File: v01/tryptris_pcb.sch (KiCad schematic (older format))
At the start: 135 parts

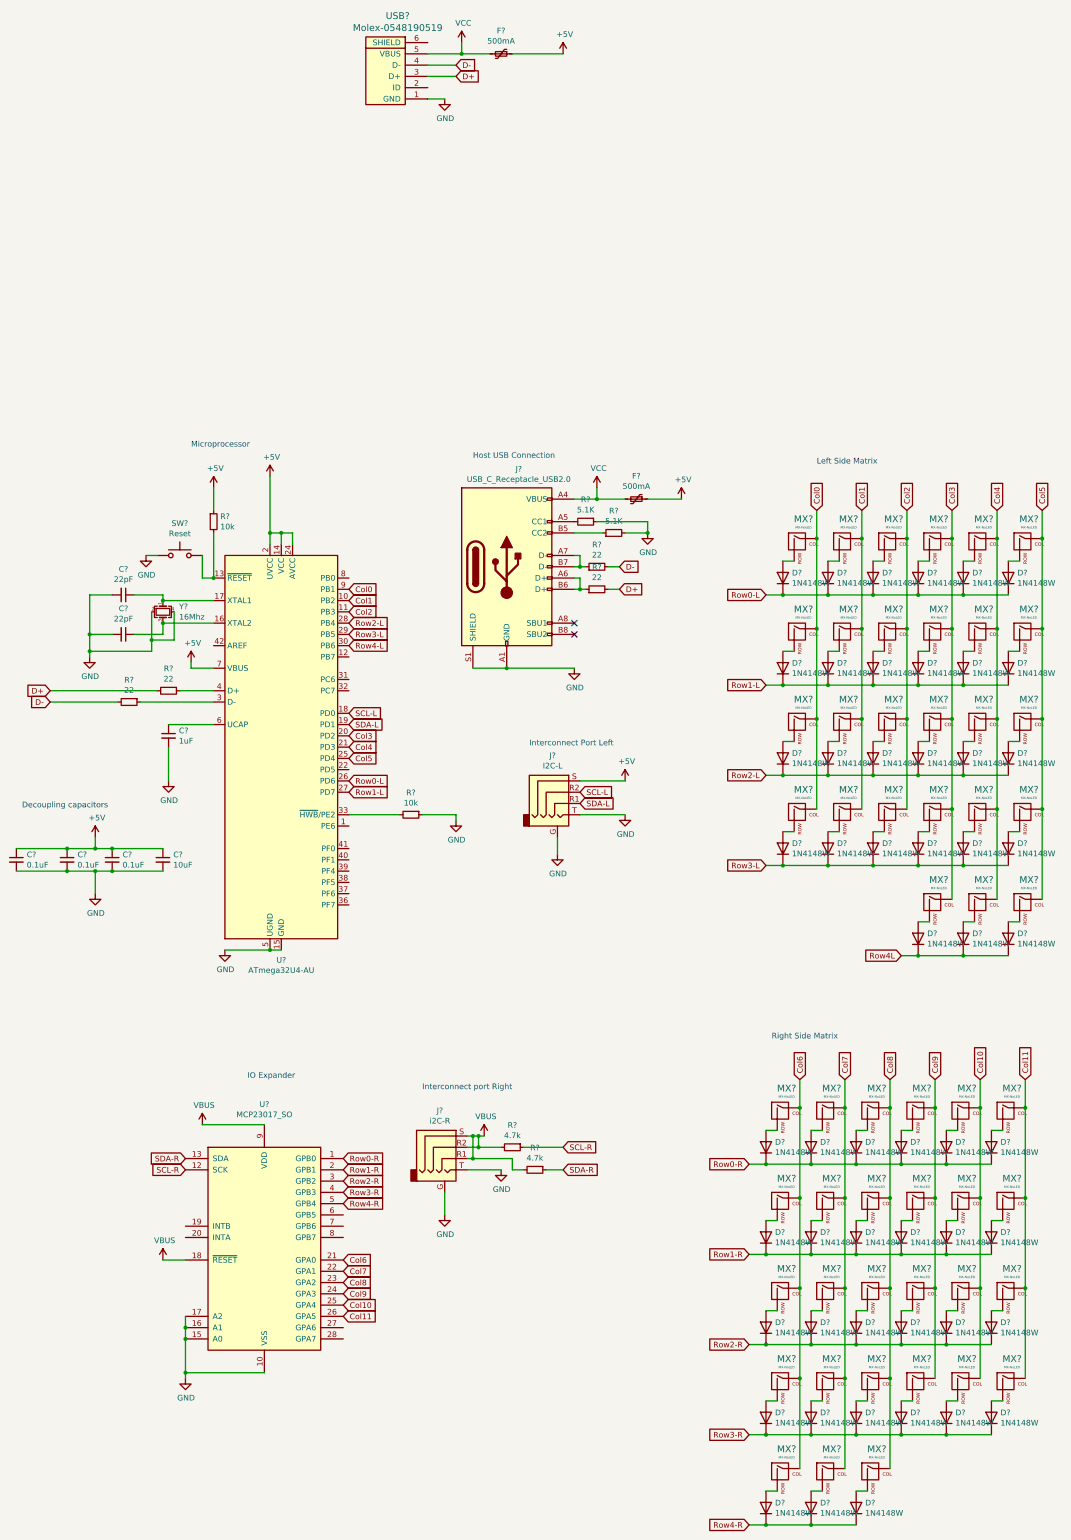
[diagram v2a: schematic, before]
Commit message: Started left side of PCB
* Got switches and diodes for the left side placed.
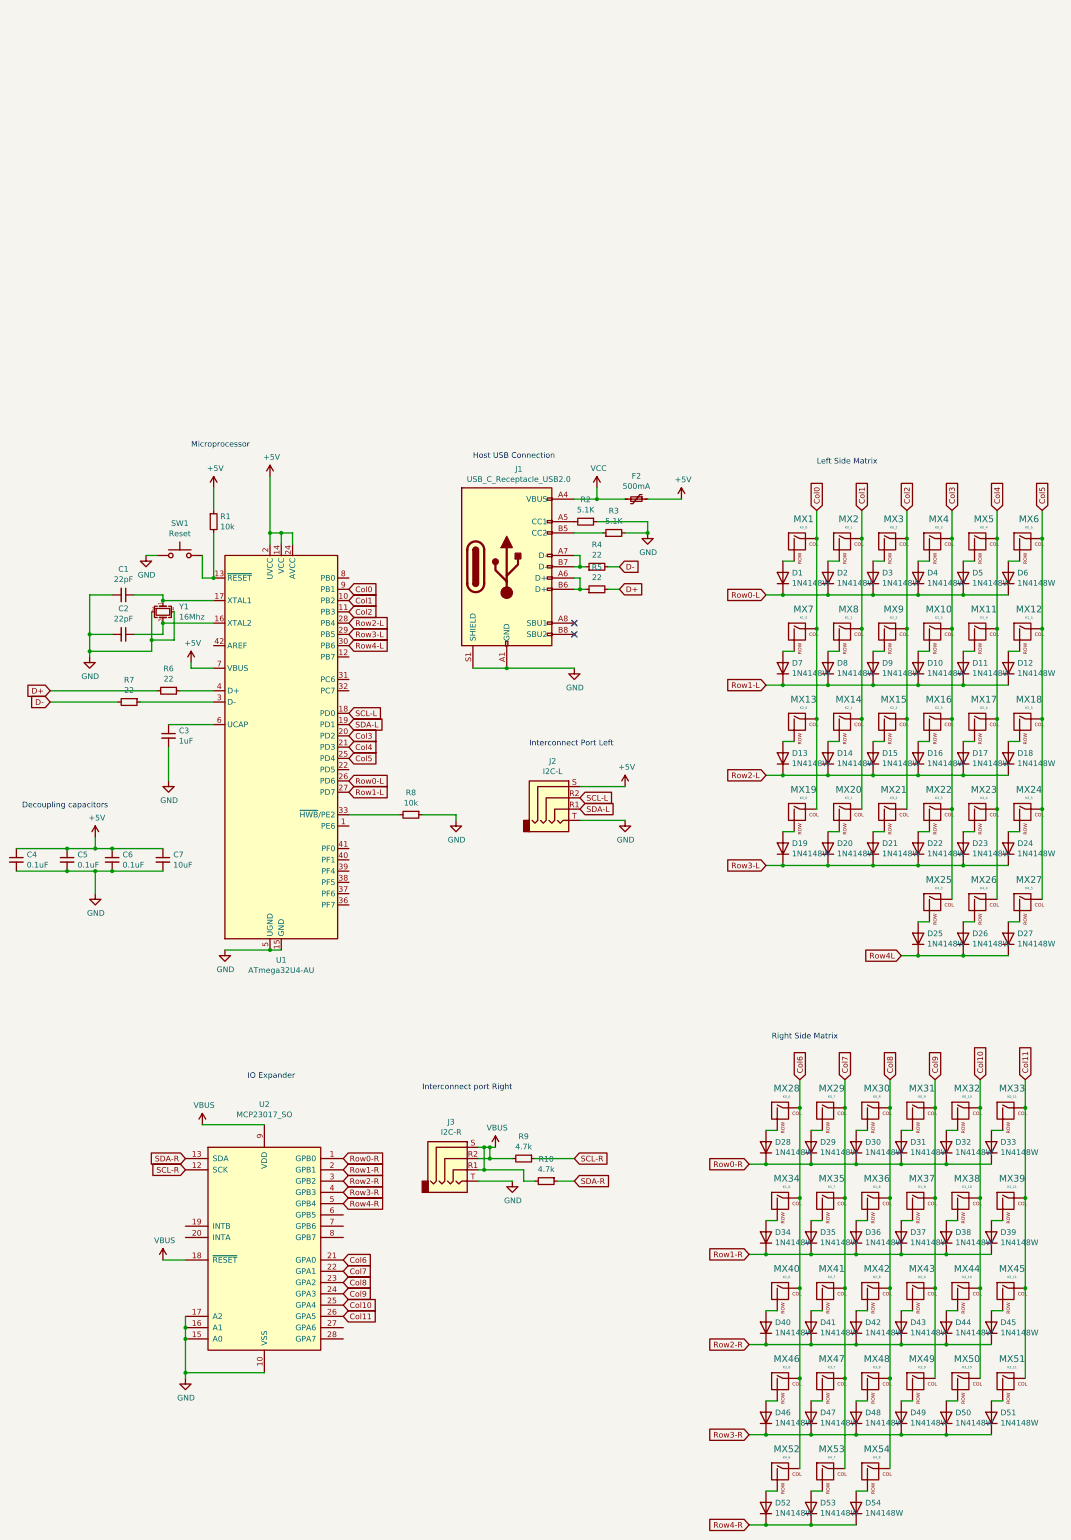
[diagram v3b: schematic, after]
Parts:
- removed F?: 500mA, symbol Device:Polyfuse_Small
- removed J?: i2C-R, symbol Connector:AudioJack4_Ground
- removed J?: I2C-L, symbol Connector:AudioJack4_Ground
- removed USB?: Molex-0548190519, symbol random-keyboard-parts:Molex-0548190519
- added J2: I2C-L, Connector_Audio:Jack_3.5mm_PJ320E_Horizontal, symbol Connector:AudioJack4
- added J3: I2C-R, Connector_Audio:Jack_3.5mm_PJ320E_Horizontal, symbol Connector:AudioJack4
- C1, C2, C3, C4, C5, C6, C7: renamed from C?; footprint (none) -> Capacitor_SMD:C_0805_2012Metric
- F2: renamed from F?; footprint (none) -> Fuse:Fuse_1206_3216Metric
- J1: renamed from J?; footprint (none) -> Type-C:USB_C_GCT_USB4085
- MX1: renamed from MX?; value MX-NoLED -> K0_0; footprint (none) -> MX_Only:MXOnly-1U-NoLED
- MX10: renamed from MX?; value MX-NoLED -> K1_3; footprint (none) -> MX_Only:MXOnly-1U-NoLED
- MX11: renamed from MX?; value MX-NoLED -> K1_4; footprint (none) -> MX_Only:MXOnly-1U-NoLED
- MX12: renamed from MX?; value MX-NoLED -> K1_5; footprint (none) -> MX_Only:MXOnly-1U-NoLED
- MX13: renamed from MX?; value MX-NoLED -> K2_0; footprint (none) -> MX_Only:MXOnly-1U-NoLED
- MX14: renamed from MX?; value MX-NoLED -> K2_1; footprint (none) -> MX_Only:MXOnly-1U-NoLED
- MX15: renamed from MX?; value MX-NoLED -> K2_2; footprint (none) -> MX_Only:MXOnly-1U-NoLED
- MX16: renamed from MX?; value MX-NoLED -> K2_3; footprint (none) -> MX_Only:MXOnly-1U-NoLED
- MX17: renamed from MX?; value MX-NoLED -> K2_4; footprint (none) -> MX_Only:MXOnly-1U-NoLED
- MX18: renamed from MX?; value MX-NoLED -> K2_5; footprint (none) -> MX_Only:MXOnly-1U-NoLED
- MX19: renamed from MX?; value MX-NoLED -> K3_0; footprint (none) -> MX_Only:MXOnly-1U-NoLED
- MX2: renamed from MX?; value MX-NoLED -> K0_1; footprint (none) -> MX_Only:MXOnly-1U-NoLED
- MX20: renamed from MX?; value MX-NoLED -> K3_1; footprint (none) -> MX_Only:MXOnly-1U-NoLED
- MX21: renamed from MX?; value MX-NoLED -> K3_2; footprint (none) -> MX_Only:MXOnly-1U-NoLED
- MX22: renamed from MX?; value MX-NoLED -> K3_3; footprint (none) -> MX_Only:MXOnly-1U-NoLED
- MX23: renamed from MX?; value MX-NoLED -> K3_4; footprint (none) -> MX_Only:MXOnly-1U-NoLED
- MX24: renamed from MX?; value MX-NoLED -> K3_5; footprint (none) -> MX_Only:MXOnly-1U-NoLED
- MX25: renamed from MX?; value MX-NoLED -> K4_3; footprint (none) -> MX_Only:MXOnly-1U-NoLED
- MX26: renamed from MX?; value MX-NoLED -> K4_4; footprint (none) -> MX_Only:MXOnly-1U-NoLED
- MX27: renamed from MX?; value MX-NoLED -> K4_5; footprint (none) -> MX_Only:MXOnly-1U-NoLED
- MX28: renamed from MX?; value MX-NoLED -> K0_6; footprint (none) -> MX_Only:MXOnly-1U-NoLED
- MX29: renamed from MX?; value MX-NoLED -> K0_7; footprint (none) -> MX_Only:MXOnly-1U-NoLED
- MX3: renamed from MX?; value MX-NoLED -> K0_2; footprint (none) -> MX_Only:MXOnly-1U-NoLED
- MX30: renamed from MX?; value MX-NoLED -> K0_8; footprint (none) -> MX_Only:MXOnly-1U-NoLED
- MX31: renamed from MX?; value MX-NoLED -> K0_9; footprint (none) -> MX_Only:MXOnly-1U-NoLED
- MX32: renamed from MX?; value MX-NoLED -> K0_10; footprint (none) -> MX_Only:MXOnly-1U-NoLED
- MX33: renamed from MX?; value MX-NoLED -> K0_11; footprint (none) -> MX_Only:MXOnly-1U-NoLED
- MX34: renamed from MX?; value MX-NoLED -> K1_6; footprint (none) -> MX_Only:MXOnly-1U-NoLED
- MX35: renamed from MX?; value MX-NoLED -> K1_7; footprint (none) -> MX_Only:MXOnly-1U-NoLED
- MX36: renamed from MX?; value MX-NoLED -> K1_8; footprint (none) -> MX_Only:MXOnly-1U-NoLED
- MX37: renamed from MX?; value MX-NoLED -> K1_9; footprint (none) -> MX_Only:MXOnly-1U-NoLED
- MX38: renamed from MX?; value MX-NoLED -> K1_10; footprint (none) -> MX_Only:MXOnly-1U-NoLED
- MX39: renamed from MX?; value MX-NoLED -> K1_11; footprint (none) -> MX_Only:MXOnly-1U-NoLED
- MX4: renamed from MX?; value MX-NoLED -> K0_3; footprint (none) -> MX_Only:MXOnly-1U-NoLED
- MX40: renamed from MX?; value MX-NoLED -> K2_6; footprint (none) -> MX_Only:MXOnly-1U-NoLED
- MX41: renamed from MX?; value MX-NoLED -> K2_7; footprint (none) -> MX_Only:MXOnly-1U-NoLED
- MX42: renamed from MX?; value MX-NoLED -> K2_8; footprint (none) -> MX_Only:MXOnly-1U-NoLED
- MX43: renamed from MX?; value MX-NoLED -> K2_9; footprint (none) -> MX_Only:MXOnly-1U-NoLED
- MX44: renamed from MX?; value MX-NoLED -> K2_10; footprint (none) -> MX_Only:MXOnly-1U-NoLED
- MX45: renamed from MX?; value MX-NoLED -> K2_11; footprint (none) -> MX_Only:MXOnly-1U-NoLED
- MX46: renamed from MX?; value MX-NoLED -> K3_6; footprint (none) -> MX_Only:MXOnly-1U-NoLED
- MX47: renamed from MX?; value MX-NoLED -> K3_7; footprint (none) -> MX_Only:MXOnly-1U-NoLED
- MX48: renamed from MX?; value MX-NoLED -> K3_8; footprint (none) -> MX_Only:MXOnly-1U-NoLED
- MX49: renamed from MX?; value MX-NoLED -> K3_9; footprint (none) -> MX_Only:MXOnly-1U-NoLED
- MX5: renamed from MX?; value MX-NoLED -> K0_4; footprint (none) -> MX_Only:MXOnly-1U-NoLED
- MX50: renamed from MX?; value MX-NoLED -> K3_10; footprint (none) -> MX_Only:MXOnly-1U-NoLED
- MX51: renamed from MX?; value MX-NoLED -> K3_11; footprint (none) -> MX_Only:MXOnly-1U-NoLED
- MX52: renamed from MX?; value MX-NoLED -> K4_6; footprint (none) -> MX_Only:MXOnly-1U-NoLED
- MX53: renamed from MX?; value MX-NoLED -> K4_7; footprint (none) -> MX_Only:MXOnly-1U-NoLED
- MX54: renamed from MX?; value MX-NoLED -> K4_8; footprint (none) -> MX_Only:MXOnly-1U-NoLED
- MX6: renamed from MX?; value MX-NoLED -> K0_5; footprint (none) -> MX_Only:MXOnly-1U-NoLED
- MX7: renamed from MX?; value MX-NoLED -> K1_0; footprint (none) -> MX_Only:MXOnly-1U-NoLED
- MX8: renamed from MX?; value MX-NoLED -> K1_1; footprint (none) -> MX_Only:MXOnly-1U-NoLED
- MX9: renamed from MX?; value MX-NoLED -> K1_2; footprint (none) -> MX_Only:MXOnly-1U-NoLED
- R1, R10, R2, R3, R4, R5, R6, R7, R8, R9: renamed from R?; footprint (none) -> Resistor_SMD:R_0805_2012Metric
- SW1: renamed from SW?; footprint (none) -> random-keyboard-parts:PushButton_6x6mm_TH
- Y1: renamed from Y?; footprint (none) -> Crystal:Crystal_SMD_3225-4Pin_3.2x2.5mm
- gave numbers to parts that had none: 56
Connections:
- net +5V: now also J2.S
- net GND: now also J2.T, J3.T
- net SCL-L: now also J2.R2
- net SDA-L: now also J2.R1
- net VBUS: now also J3.R1, J3.R2, J3.S
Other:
- moved on the sheet: R10, R9

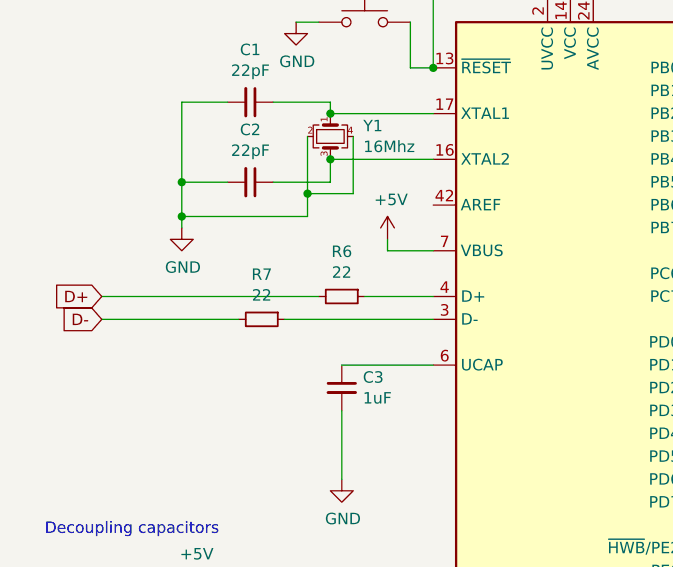
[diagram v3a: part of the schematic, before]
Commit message: PCB components roughly placed
* Removed duplicate resistors on D- and D+
* Roughly placed all components. MCU and IO expander and resistors are
  all on the back to save board space. I'm hoping that the board can fit
  inside the existing switch place outline.
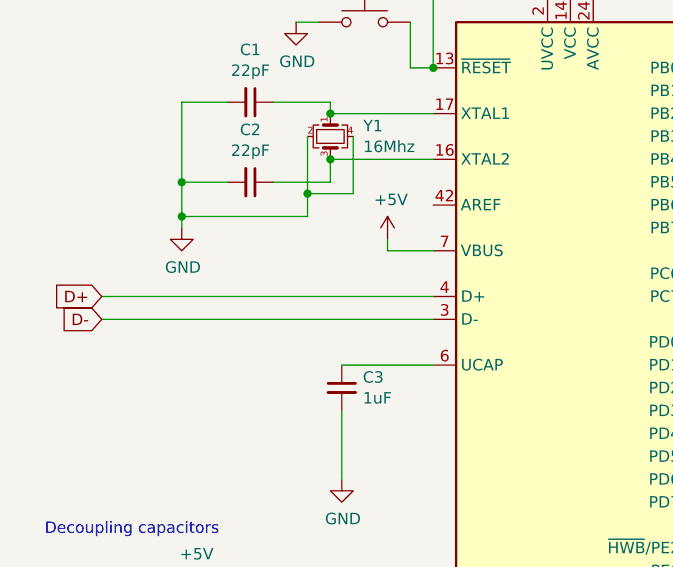
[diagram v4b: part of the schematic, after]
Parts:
- removed R6, R7: 22, Resistor_SMD:R_0805_2012Metric, symbol Device:R_Small
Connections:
- net D+: now also U1.4 (D+)
- net D-: now also U1.3 (D-)
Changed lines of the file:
@@
 	4150 3850 3700 3850
-$Comp
-L Device:R_Small R7
-U 1 1 60F2DBF1
-P 1750 2850
-F 0 "R7" V 1554 2850 50  0000 C CNN
-F 1 "22" V 1645 2850 50  0000 C CNN
-F 2 "Resistor_SMD:R_0805_2012Metric" H 1750 2850 50  0001 C CNN
-F 3 "~" H 1750 2850 50  0001 C CNN
-	1    1750 2850
-	0    1    1    0
-$EndComp
-$Comp
-L Device:R_Small R6
-U 1 1 60F30360
-P 2100 2750
-F 0 "R6" V 1904 2750 50  0000 C CNN
-F 1 "22" V 1995 2750 50  0000 C CNN
-F 2 "Resistor_SMD:R_0805_2012Metric" H 2100 2750 50  0001 C CNN
-F 3 "~" H 2100 2750 50  0001 C CNN
-	1    2100 2750
-	0    1    1    0
-$EndComp
-Wire Wire Line
-	2200 2750 2500 2750
-Wire Wire Line
-	1850 2850 2500 2850
-Wire Wire Line
-	1650 2850 1050 2850
-Wire Wire Line
-	2000 2750 1050 2750
 $Comp
 L Device:C_Small C3
@@
 	1    0    0    -1
 $EndComp
+Wire Wire Line
+	1050 2850 2500 2850
+Wire Wire Line
+	1050 2750 2500 2750
 $EndSCHEMATC
